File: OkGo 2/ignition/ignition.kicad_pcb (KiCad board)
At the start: 2 copper layers, 167.9 x 105.9 mm, 103 parts, among them K201 16A SPST, K202 16A SPST, K203 16A SPST, K204 16A SPST, K205 16A SPST, M3_MOUNT VAL**, P105 BATT, P106 SMA, P107 ARM_LED, P109 BUZZ, P201 CH3_LED, P203 CH3, P204 CH1_LED, P206 CH1, P207 CH4_LED, P209 CH4, P210 CH2_LED, P212 CH2, Q101 BSS138BK, Q201 BSS138BK, Q202 BSS138BK, Q203 BSS138BK, Q204 BSS138BK, Q205 BSS138BK, U103 SWD, U105 RFM95W, U106 STM32F071CBT6, U107 TSR 0.5-2433, Y101 8MHz

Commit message: More footprints, partial #9
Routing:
- net GND: track 129.3 -> 132.6 mm, vias 18 -> 20
- net Net-(D103-Pad1): track 14.4 -> 16.3 mm
- net /RFM_RESET: track 46.1 -> 47.5 mm
- net /RFM_NSS: track 42.8 -> 44.2 mm
- net /RFM_MOSI: track 33.3 -> 34.7 mm
- net /RFM_DIO0: track 36.7 -> 38.1 mm
- net /RFM_DIO3: track 34.3 -> 35.7 mm
- added copper zone on F.Cu, net GND

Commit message: Penultimate footprinting, partial #9
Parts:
- added P111: SMA, ignition:SMA_upright, F.Cu at (73.7, 58.8)
- moved D103 4.18 mm to (78.7, 57.6), turned to 90 degrees
- moved P106 3.24 mm to (73.6, 51.6)
- moved C109 2.24 mm to (82.8, 62.2)
- moved C108 2.17 mm to (80.4, 62.1)
- moved C104 0.59 mm to (65.6, 80.5)
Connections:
- U103 pad 6: Net-(U103-Pad6) -> (no net)
- U103 pad 7: Net-(U103-Pad7) -> (no net)
- U103 pad 8: Net-(U103-Pad8) -> (no net)
- U106 pad 11: Net-(U106-Pad11) -> (no net)
- U106 pad 12: Net-(U106-Pad12) -> (no net)
- U106 pad 13: Net-(U106-Pad13) -> (no net)
- U106 pad 20: Net-(U106-Pad20) -> (no net)
- U106 pad 21: Net-(U106-Pad21) -> (no net)
- U106 pad 22: Net-(U106-Pad22) -> (no net)
- U106 pad 25: Net-(U106-Pad25) -> (no net)
- U106 pad 26: Net-(U106-Pad26) -> (no net)
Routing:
- net GND: track 132.6 -> 163.3 mm, vias 20 -> 16
- net Net-(D103-Pad1): track 16.3 -> 23.0 mm

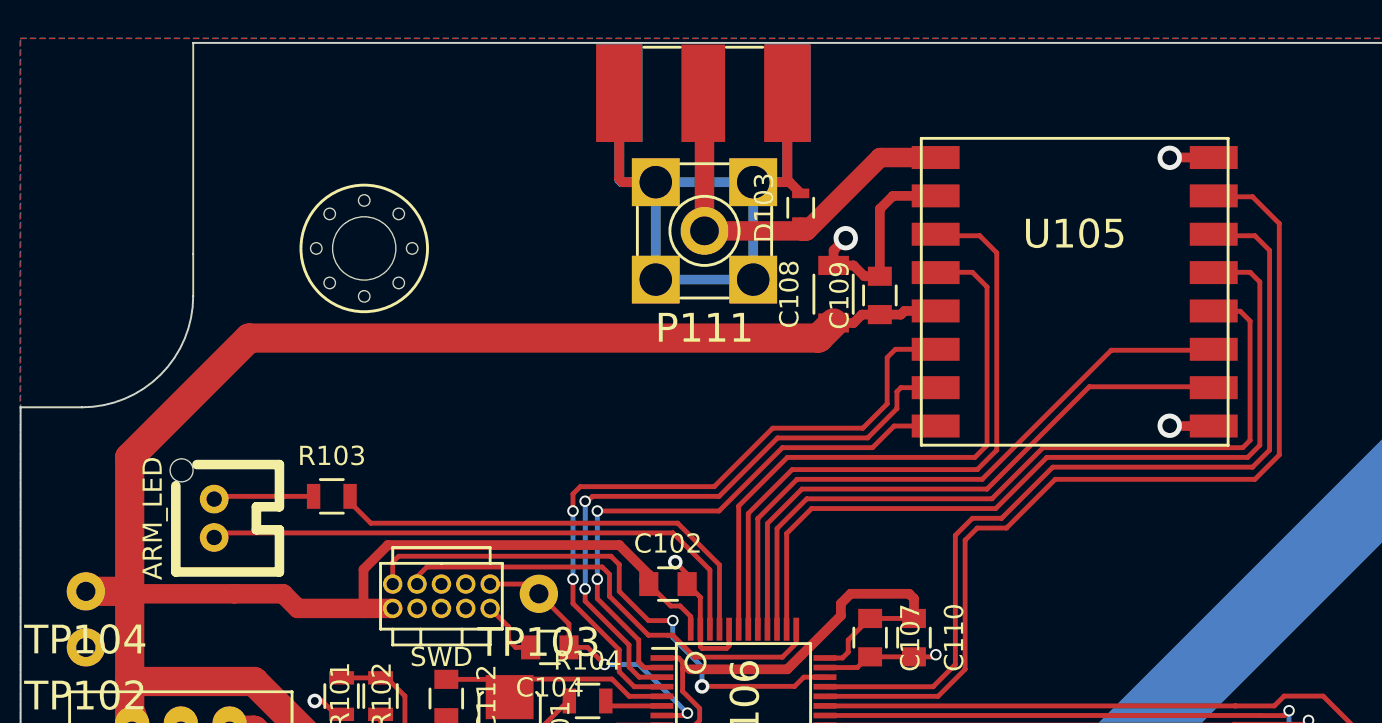
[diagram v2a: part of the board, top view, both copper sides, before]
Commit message: Finished footprinting, resolves #9
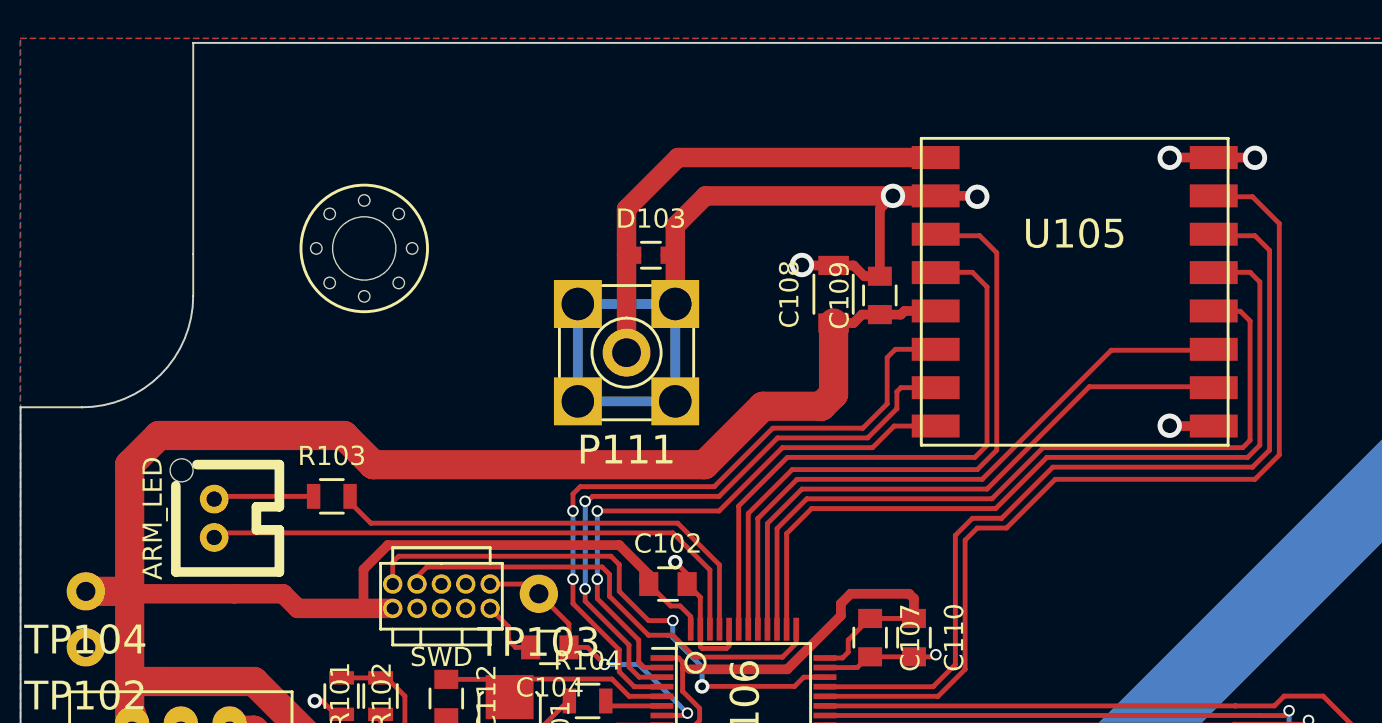
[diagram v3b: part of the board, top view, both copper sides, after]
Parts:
- removed P106: SMA, common:SMA-142-0701-801
- moved D103 8.19 mm to (70.9, 60.1), turned to 0 degrees
- moved P111 7.54 mm to (69.6, 65.2)
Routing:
- net Net-(D103-Pad1): track 23.0 -> 27.1 mm
- net GND: track 163.3 -> 160.2 mm, vias 16 -> 19
- net +3V3: track 386.7 -> 389.8 mm

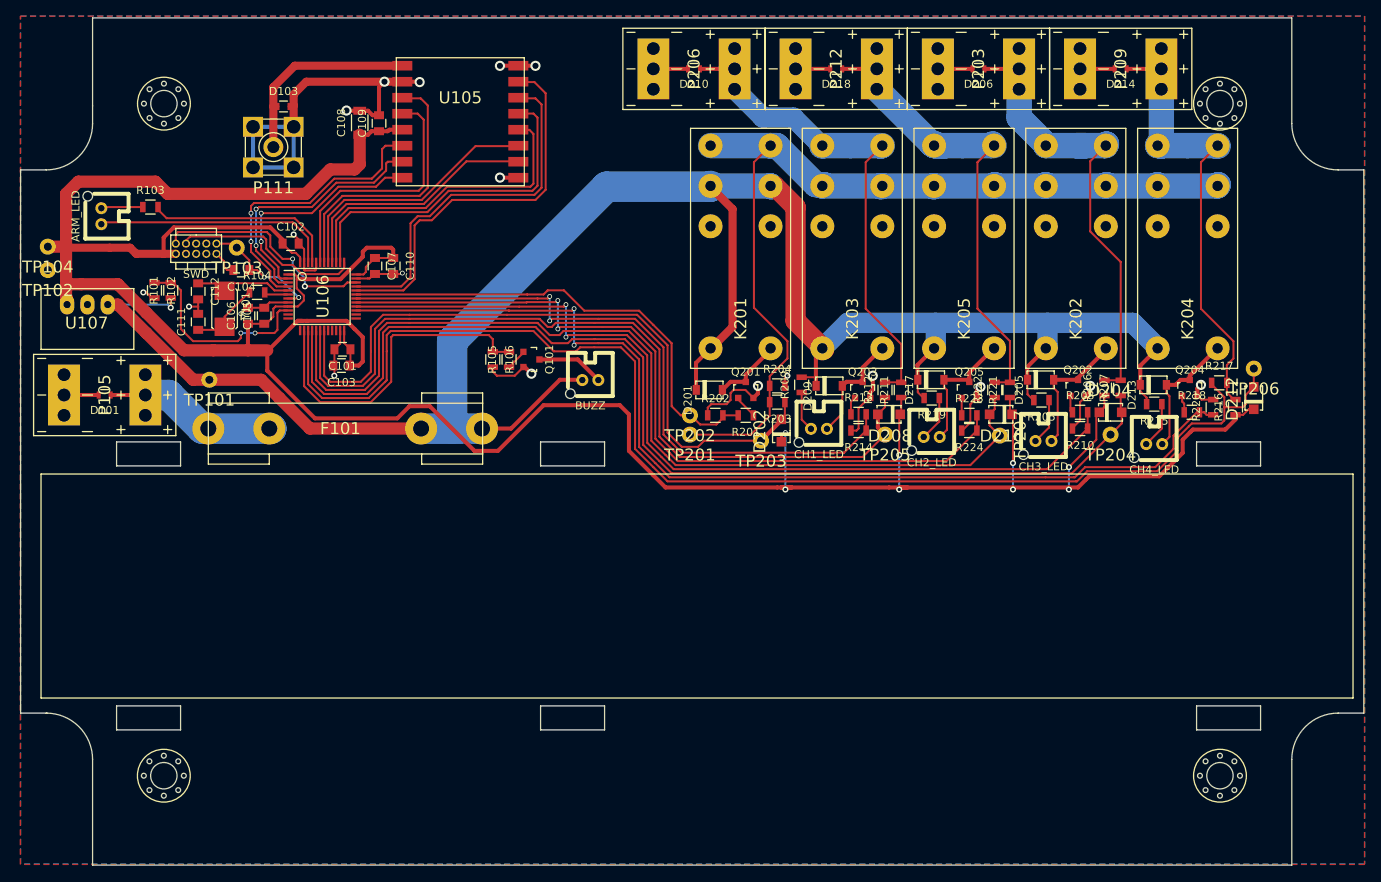
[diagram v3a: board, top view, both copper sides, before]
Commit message: Chunkied vias, rerouted some bits, resolves #36
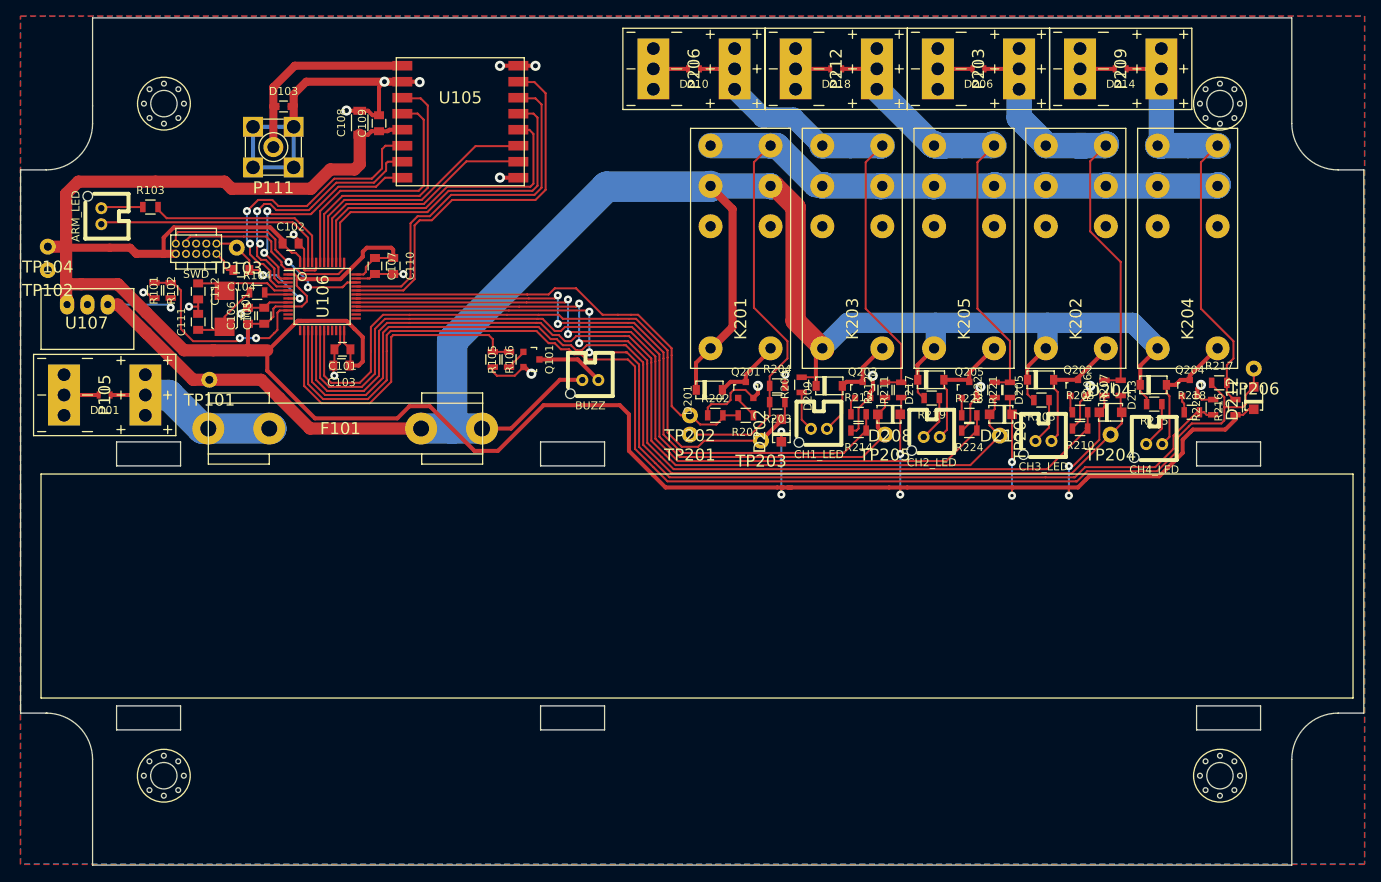
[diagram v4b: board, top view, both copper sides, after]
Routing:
- net +3V3: track 389.8 -> 395.3 mm
- net /RFM_DIO0: track 38.1 -> 39.3 mm
- net /RFM_DIO1: track 34.4 -> 35.3 mm
- net /firing/CONT_CH4: track 160.5 -> 159.8 mm
- net /SWDIO: track 28.9 -> 28.2 mm
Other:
- net class Default: clearance 0.2 -> 0.19812; trace_width 0.25 -> 0.254; via_dia 0.6 -> 1.016; via_drill 0.4 -> 0.4064
- rule trace_clearance: 0.2 -> 0.19812
- rule trace_min: 0.2 -> 0.2032
- rule via_min_drill: 0.3 -> 0.4064
- rule via_min_size: 0.4 -> 1.016

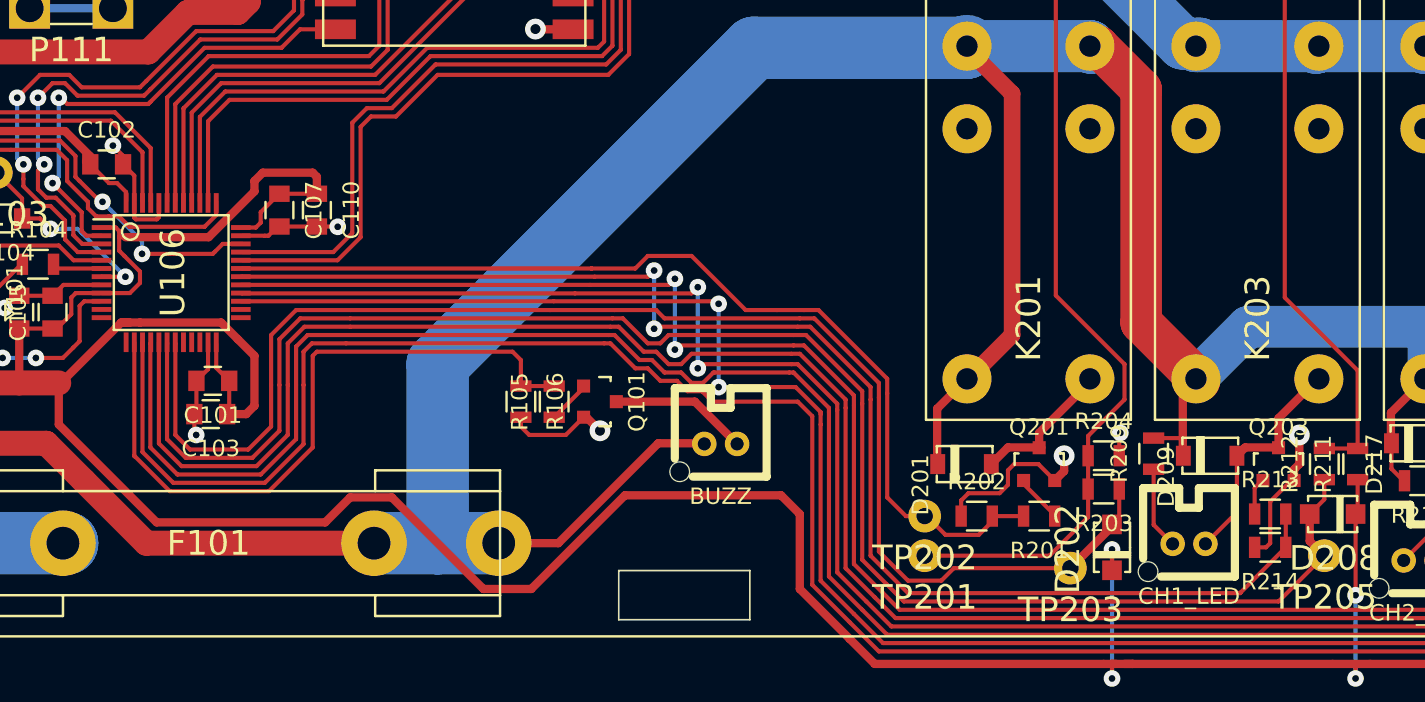
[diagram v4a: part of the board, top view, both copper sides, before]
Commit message: Added LEDs to ignition
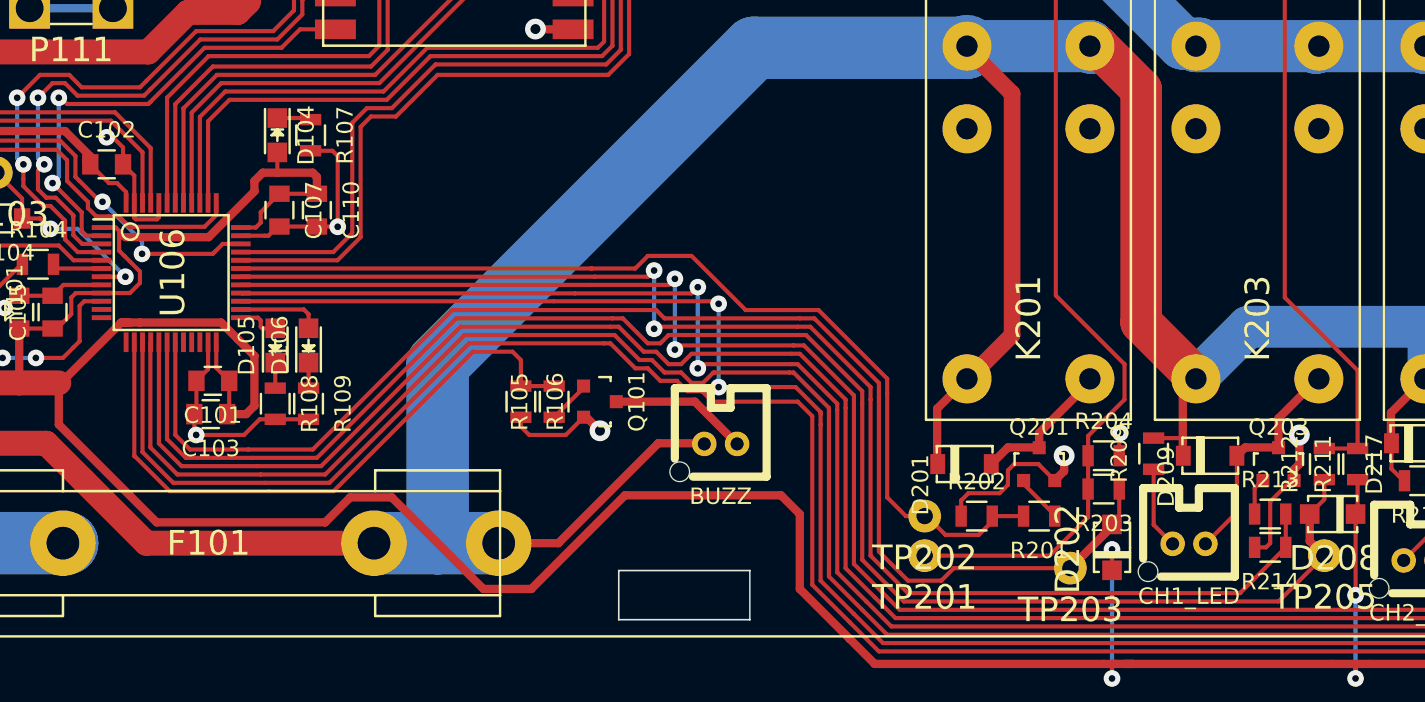
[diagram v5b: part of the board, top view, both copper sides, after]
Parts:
- added D104: RED, LEDs:LED-0805, F.Cu at (82.2, 75.4)
- added D105: GREEN, LEDs:LED-0805, F.Cu at (82.0, 88.3)
- added D106: YELLOW, LEDs:LED-0805, F.Cu at (84.1, 88.3)
- added R107: R, Resistors_SMD:R_0805, F.Cu at (84.2, 75.4)
- added R108: R, Resistors_SMD:R_0805, F.Cu at (82.0, 91.8)
- added R109: R, Resistors_SMD:R_0805, F.Cu at (84.1, 91.8)
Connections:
- U106 pad 25: (no net) -> Net-(D105-Pad2)
- U106 pad 26: (no net) -> Net-(D106-Pad2)
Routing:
- net GND: track 160.4 -> 174.6 mm
- net Net-(D106-Pad2): track 0.00 -> 5.11 mm
- net /firing/CONT_CH4: track 159.8 -> 156.5 mm
- net /firing/CONT_CH3: track 135.4 -> 132.1 mm
- net /firing/RELAY_SENSE: track 86.8 -> 83.5 mm
- net /firing/CONT_CH2: track 120.0 -> 116.7 mm
- net /firing/CONT_CH1: track 104.1 -> 100.8 mm
- net /BUZZER: track 42.1 -> 38.8 mm
- net Net-(D105-Pad2): track 0.00 -> 2.59 mm
- net Net-(D104-Pad1): track 0.00 -> 2.07 mm
- net Net-(D106-Pad1): track 0.00 -> 1.56 mm
- net Net-(D105-Pad1): track 0.00 -> 1.56 mm
- net +3V3: track 395.3 -> 396.5 mm

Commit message: Ignition copper tidying
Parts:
- moved P109 10.6 mm to (99.6, 89.0)
- moved R106 9.00 mm to (105.7, 94.2)
- moved R105 5.23 mm to (103.6, 94.2)
- moved Q101 2.74 mm to (100.8, 94.2), turned to 90 degrees
- moved TP101 1.66 mm to (61.7, 92.6)
- moved Y101 0.38 mm to (63.1, 83.3)
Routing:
- net /BUZZER: track 38.8 -> 47.4 mm
- net GND: track 174.6 -> 181.2 mm
- net Net-(P109-Pad1): track 8.44 -> 4.71 mm
- net /firing/CONT_CH3: track 132.1 -> 129.6 mm
- net /firing/CONT_CH2: track 116.7 -> 114.3 mm
- net +BATT: track 272.4 -> 270.0 mm
- net /firing/CONT_CH1: track 100.8 -> 98.6 mm
- net /firing/FIRE_CH4: track 129.2 -> 127.0 mm
- net /firing/RELAY_SENSE: track 83.5 -> 81.6 mm
- net /firing/UPSTREAM_RELAY: track 60.2 -> 58.4 mm
- net /firing/CONT_CH4: track 156.5 -> 154.7 mm
- net +3V3: track 396.5 -> 398.3 mm
- net /firing/FIRE_CH3: track 113.7 -> 112.0 mm
- net Net-(Q201-Pad1): track 2.95 -> 4.13 mm
- net /firing/FIRE_CH1: track 83.6 -> 82.5 mm
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
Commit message: Ignition: Tidying, GND stitching, finishing
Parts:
- added G***: LOGO, common:cusf_logo_full_huge, B.Cu at (63.0, 125.9)
- added G***: LOGO, ignition:wile_e_rocket, B.Cu at (157.6, 123.7)
- added G***: LOGO, ignition:cusf_rocket_big, F.Cu at (199.8, 86.7)
- moved D205 0.38 mm to (165.6, 94.6)
- moved D217 0.25 mm to (151.9, 94.5)
- moved R205 0.25 mm to (165.6, 97.0)
- moved R219 0.25 mm to (151.9, 96.8)
- moved K201 0.25 mm to (128.0, 78.0)
- moved K202 0.25 mm to (169.9, 78.0)
- moved K203 0.25 mm to (142.0, 78.0)
- moved K204 0.25 mm to (183.9, 78.0)
- moved K205 0.25 mm to (156.0, 78.0)
- moved P210 0.25 mm to (151.9, 100.8)
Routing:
- net GND: track 181.2 -> 1436.7 mm, vias 19 -> 150
- net (no net): track 0.00 -> 74.7 mm, vias 0 -> 4
- net Net-(D206-Pad1): track 62.6 -> 60.0 mm
- net /firing/FIRING_DIST: track 117.2 -> 115.1 mm
- net +3V3: track 398.3 -> 396.5 mm
- net Net-(D218-Pad1): track 63.9 -> 62.3 mm
- net +BATT: track 270.0 -> 270.8 mm
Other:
- board text added: "+3v3"
- board text added: "+BATT"
- board text added: "15A 6.3x32 mm"
- board text added: "3v3"
- board text added: "ARM LED"
- board text added: "BATTERY"
- board text added: "BUZZER"
- board text added: "CH1"
- board text added: "CH1 LED"
- board text added: "CH2"
- board text added: "CH2 LED"
- board text added: "CH3"
- board text added: "CH3 LED"
- board text added: "CH4"
- board text added: "CH4 LED"
- board text added: "CONT CH1"
- board text added: "CONT CH2"
- board text added: "CONT CH4"
- board text added: "DAVID TURNER 2015-08-19"
- board text added: "FIRING DIST"
- board text added: "GND"
- board text added: "OkGo 2 IGNITION"
- board text added: "RELAY SENSE"
- board text added: "RESET"
- board text added: "UPSTREAM RELAY"
